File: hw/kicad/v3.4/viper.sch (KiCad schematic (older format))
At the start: 15 parts

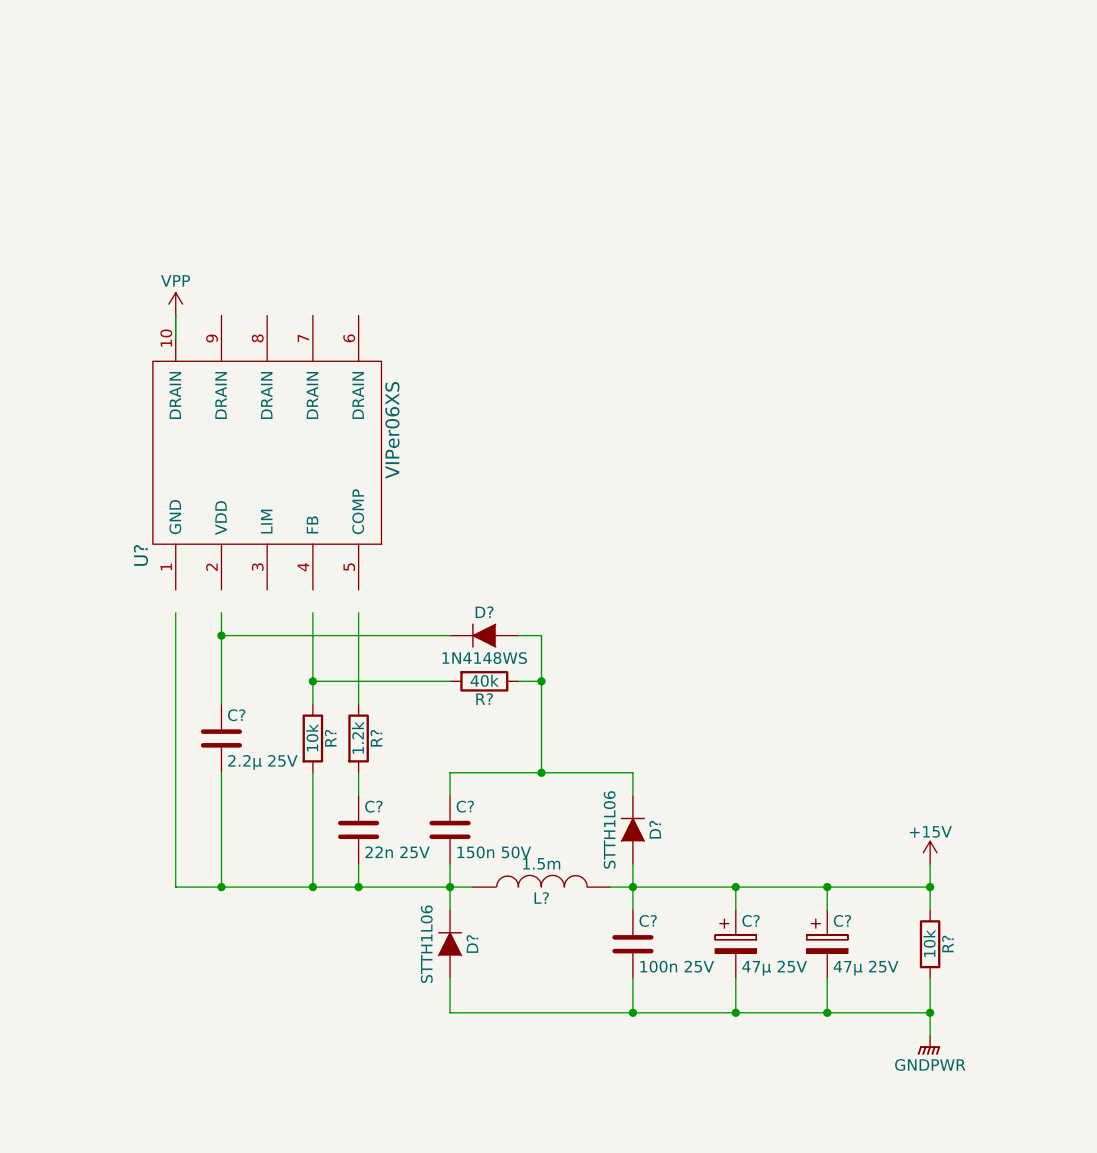
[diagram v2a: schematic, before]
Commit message: +f1 3.3V, viper fix
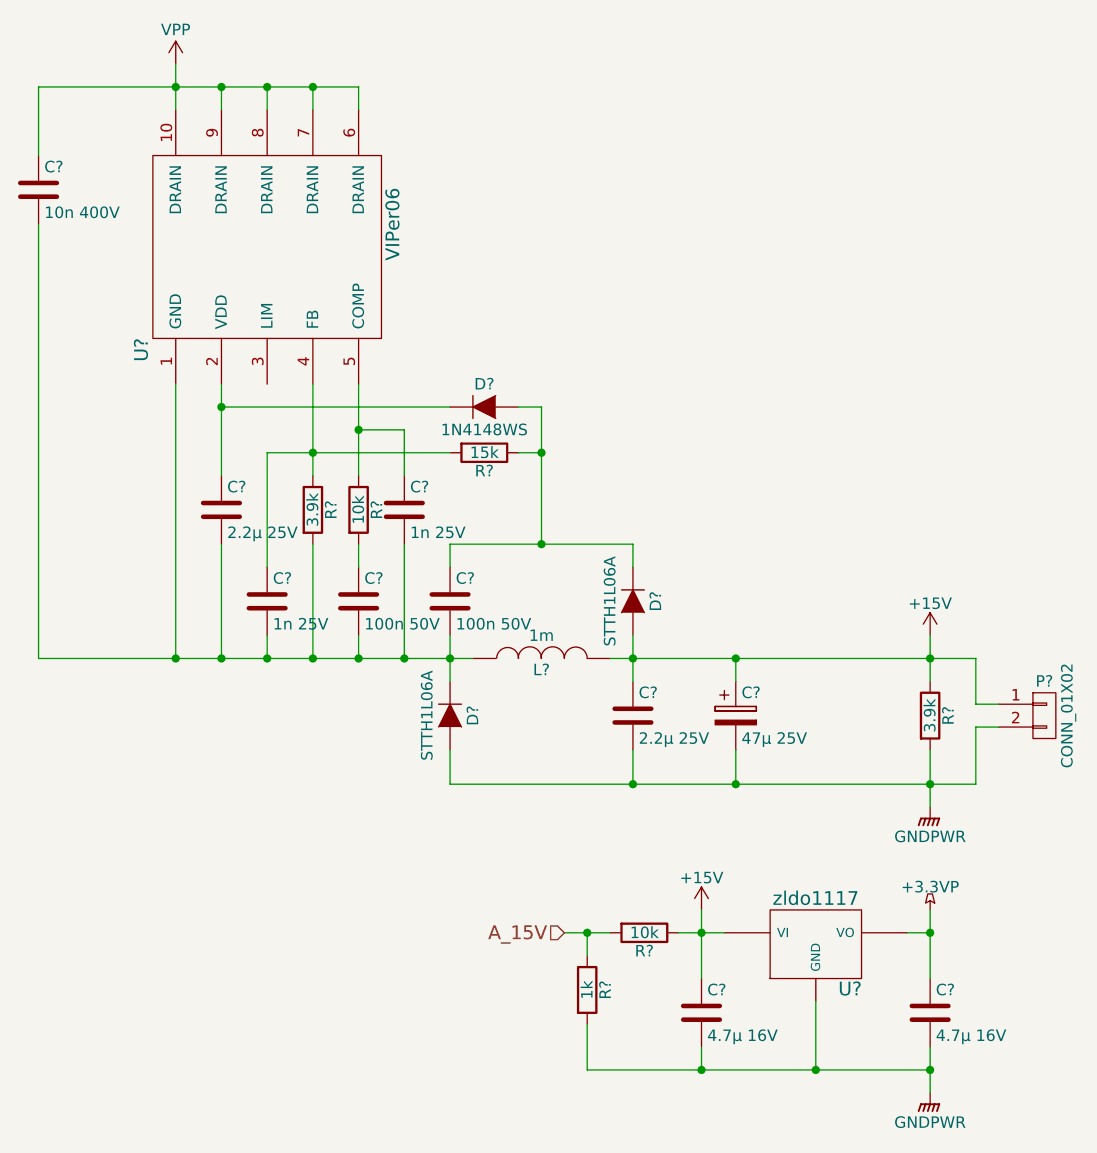
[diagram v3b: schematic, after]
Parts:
- removed C?: 47µ 25V, symbol CP
- added C?: 10n 400V, symbol C
- added C? (x2): 1n 25V, symbol C
- added C? (x2): 4.7µ 16V, symbol C
- added P?: CONN_01X02, symbol CONN_01X02
- added R?: 10k, symbol R
- added R?: 1k, symbol R
- added U?: zldo1117, symbol LM7812
- C?: value 150n 50V -> 100n 50V
- C?: value 100n 25V -> 2.2µ 25V
- C?: value 22n 25V -> 100n 50V
- D? (x2): value STTH1L06 -> STTH1L06A
- L?: value 1.5m -> 1m
- R?: value 1.2k -> 10k
- R? (x2): value 10k -> 3.9k
- R?: value 40k -> 15k
- U?: value VIPer06XS -> VIPer06
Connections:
- net labels added: +3.3VP, A_15V
- wire segments 30 -> 55
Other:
- moved on the sheet: C?, D?, L?, R?, U?

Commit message: hw v3.4
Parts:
- removed C?: 4.7µ 16V, symbol C
- added C?: 4.7µ, symbol C
- C? (x2): value 2.2µ 25V -> 2.2µ; Voltage (none) -> 25V
- C? (x2): value 100n 50V -> 100n
- C?: value 47µ 25V -> 47µ; Voltage (none) -> 25V
- C?: value 1n 25V -> 1n; Voltage (none) -> 25V
- C?: value 4.7µ 16V -> 4.7µ; Voltage (none) -> 25V
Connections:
- net +3.3VP: now also C?.1
- net GNDPWR: now also C?.2
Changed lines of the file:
@@
 EESchema Schematic File Version 2
 LIBS:conn
+LIBS:power
 LIBS:stmbl_3.4-cache
 EELAYER 25 0
@@
 P 5400 3350
 F 0 "C?" H 5425 3450 50  0000 L CNN
-F 1 "2.2µ 25V" H 5425 3250 50  0000 L CNN
+F 1 "2.2µ" H 5425 3250 50  0000 L CNN
 F 2 "" H 5438 3200 30  0000 C CNN
 F 3 "" H 5400 3350 60  0000 C CNN
+F 4 "25V" H 5400 3350 60  0001 C CNN "Voltage"
 	1    5400 3350
 	1    0    0    -1
@@
 P 6400 3750
 F 0 "C?" H 6425 3850 50  0000 L CNN
-F 1 "100n 50V" H 6425 3650 50  0000 L CNN
+F 1 "100n" H 6425 3650 50  0000 L CNN
 F 2 "" H 6438 3600 30  0000 C CNN
 F 3 "" H 6400 3750 60  0000 C CNN
@@
 P 7200 4250
 F 0 "C?" H 7225 4350 50  0000 L CNN
-F 1 "2.2µ 25V" H 7225 4150 50  0000 L CNN
+F 1 "2.2µ" H 7225 4150 50  0000 L CNN
 F 2 "" H 7238 4100 30  0000 C CNN
 F 3 "" H 7200 4250 60  0000 C CNN
+F 4 "25V" H 7200 4250 60  0001 C CNN "Voltage"
 	1    7200 4250
 	1    0    0    -1
@@
 P 7650 4250
 F 0 "C?" H 7675 4350 50  0000 L CNN
-F 1 "47µ 25V" H 7675 4150 50  0000 L CNN
+F 1 "47µ" H 7675 4150 50  0000 L CNN
 F 2 "" H 7688 4100 30  0000 C CNN
 F 3 "" H 7650 4250 60  0000 C CNN
+F 4 "25V" H 7650 4250 60  0001 C CNN "Voltage"
 	1    7650 4250
 	1    0    0    -1
@@
 P 6000 3750
 F 0 "C?" H 6025 3850 50  0000 L CNN
-F 1 "100n 50V" H 6025 3650 50  0000 L CNN
+F 1 "100n" H 6025 3650 50  0000 L CNN
 F 2 "" H 6038 3600 30  0000 C CNN
 F 3 "" H 6000 3750 60  0000 C CNN
@@
 P 5600 3750
 F 0 "C?" H 5625 3850 50  0000 L CNN
-F 1 "1n 25V" H 5625 3650 50  0000 L CNN
+F 1 "1n" H 5625 3650 50  0000 L CNN
 F 2 "" H 5638 3600 30  0000 C CNN
 F 3 "" H 5600 3750 60  0000 C CNN
+F 4 "25V" H 5600 3750 60  0001 C CNN "Voltage"
 	1    5600 3750
 	1    0    0    -1
@@
 $Comp
 L C C?
-U 1 1 566D4BF3
-P 8500 5550
-F 0 "C?" H 8525 5650 50  0000 L CNN
-F 1 "4.7µ 16V" H 8525 5450 50  0000 L CNN
-F 2 "" H 8538 5400 30  0000 C CNN
-F 3 "" H 8500 5550 60  0000 C CNN
-	1    8500 5550
-	1    0    0    -1
-$EndComp
-$Comp
-L C C?
 U 1 1 566D4BFA
 P 7500 5550
 F 0 "C?" H 7525 5650 50  0000 L CNN
-F 1 "4.7µ 16V" H 7525 5450 50  0000 L CNN
+F 1 "4.7µ" H 7525 5450 50  0000 L CNN
 F 2 "" H 7538 5400 30  0000 C CNN
 F 3 "" H 7500 5550 60  0000 C CNN
+F 4 "25V" H 7500 5550 60  0001 C CNN "Voltage"
 	1    7500 5550
 	1    0    0    -1
@@
 Connection ~ 7500 5800
 Connection ~ 7000 5200
+$Comp
+L C C?
+U 1 1 5681ECD1
+P 8500 5550
+F 0 "C?" H 8525 5650 50  0000 L CNN
+F 1 "4.7µ" H 8525 5450 50  0000 L CNN
+F 2 "" H 8538 5400 30  0000 C CNN
+F 3 "" H 8500 5550 60  0000 C CNN
+F 4 "25V" H 8500 5550 60  0001 C CNN "Voltage"
+	1    8500 5550
+	1    0    0    -1
+$EndComp
 $EndSCHEMATC

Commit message: hw v3.4 +testpoints
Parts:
- added T? (x3): testpoint, symbol testpoint
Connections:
- net +15V: now also T?.1
- net +3.3VP: now also T?.1
- net GNDPWR: now also T?.1
- net A_15V: no longer names the net of R?.1, R?.2
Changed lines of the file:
@@
 EESchema Schematic File Version 2
-LIBS:conn
 LIBS:power
 LIBS:stmbl_3.4-cache
@@
 Connection ~ 7500 5200
 Wire Wire Line
-	8400 5200 8500 5200
+	8400 5200 8600 5200
 Wire Wire Line
 	8500 5100 8500 5400
@@
 	7400 5200 7600 5200
 Wire Wire Line
-	7000 5800 8500 5800
+	7000 5800 8600 5800
 Connection ~ 8500 5800
 $Comp
@@
 	1    0    0    -1
 $EndComp
-Text HLabel 6900 5200 0    60   Input ~ 0
-A_15V
 $Comp
 L R R?
@@
 $EndComp
 Wire Wire Line
-	6900 5200 7100 5200
-Wire Wire Line
 	7000 5200 7000 5300
 Wire Wire Line
 	7000 5600 7000 5800
 Connection ~ 7500 5800
-Connection ~ 7000 5200
 $Comp
 L C C?
@@
 	1    0    0    -1
 $EndComp
+$Comp
+L testpoint T?
+U 1 1 56822428
+P 7650 3800
+F 0 "T?" H 7650 3900 60  0000 C CNN
+F 1 "testpoint" H 7650 3700 60  0000 C CNN
+F 2 "" H 7650 3800 60  0000 C CNN
+F 3 "" H 7650 3800 60  0000 C CNN
+	1    7650 3800
+	0    -1   -1   0
+$EndComp
+$Comp
+L testpoint T?
+U 1 1 568224B7
+P 8800 5200
+F 0 "T?" H 8800 5300 60  0000 C CNN
+F 1 "testpoint" H 8800 5100 60  0000 C CNN
+F 2 "" H 8800 5200 60  0000 C CNN
+F 3 "" H 8800 5200 60  0000 C CNN
+	1    8800 5200
+	1    0    0    -1
+$EndComp
+Wire Wire Line
+	7000 5200 7100 5200
+$Comp
+L testpoint T?
+U 1 1 5682FEC2
+P 8800 5800
+F 0 "T?" H 8800 5900 60  0000 C CNN
+F 1 "testpoint" H 8800 5700 60  0000 C CNN
+F 2 "" H 8800 5800 60  0000 C CNN
+F 3 "" H 8800 5800 60  0000 C CNN
+	1    8800 5800
+	1    0    0    -1
+$EndComp
